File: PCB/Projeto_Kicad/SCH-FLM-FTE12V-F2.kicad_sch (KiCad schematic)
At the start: 17 parts, among them CN1 AKZ700-2-5,08V, CN2 AKZ700-2-5,08V, Q1 TIP120, Q2 BC547

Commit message: Atualização do resistor shunt R2 e R4
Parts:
- added R4: 0,22R/5W, Resistor_THT:R_Axial_DIN0516_L15.5mm_D5.0mm_P5.08mm_Vertical, symbol Device:R_US
- C1, C5: value 4700uF/25V -> 4700uF/35V
- R2: value 0,44R/5W -> 0,33R/5W
- RV1: value 10K -> 11K
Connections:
- net Vout: now also R4.2; no longer R2.2
- net +15V renamed +18V
- new net: R2.2, R4.1
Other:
- moved on the sheet: R2
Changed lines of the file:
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@@
+	)
+	(junction
+		(at 266.7 128.27)
+		(diameter 0)
+		(color 0 0 0 0)
 	)
 	(junction
@@
 	)
 	(junction
-		(at 299.72 128.27)
-		(diameter 0)
-		(color 0 0 0 0)
-	)
-	(junction
 		(at 220.98 154.94)
 		(diameter 0)
@@
 	)
 	(junction
-		(at 266.7 128.27)
-		(diameter 0)
-		(color 0 0 0 0)
-	)
-	(junction
 		(at 168.91 154.94)
 		(diameter 0)
@@
 	)
 	(junction
+		(at 299.72 128.27)
+		(diameter 0)
+		(color 0 0 0 0)
+	)
+	(junction
 		(at 199.39 139.7)
 		(diameter 0)
@@
 	(wire
 		(pts
+			(xy 279.4 128.27) (xy 287.02 128.27)
+		)
+		(stroke
+			(width 0)
+			(type default)
+		)
+	)
+	(wire
+		(pts
 			(xy 196.85 154.94) (xy 199.39 154.94)
 		)
@@
 	(wire
 		(pts
-			(xy 266.7 128.27) (xy 275.59 128.27)
+			(xy 266.7 128.27) (xy 271.78 128.27)
+		)
+		(stroke
+			(width 0)
+			(type default)
+		)
+	)
+	(wire
+		(pts
+			(xy 294.64 128.27) (xy 299.72 128.27)
 		)
 		(stroke
@@
 		(pts
 			(xy 177.8 148.59) (xy 177.8 154.94)
-		)
-		(stroke
-			(width 0)
-			(type default)
-		)
-	)
-	(wire
-		(pts
-			(xy 283.21 128.27) (xy 299.72 128.27)
 		)
 		(stroke
@@
 			)
 		)
-		(property "Value" "4700uF/25V"
+		(property "Value" "4700uF/35V"
 			(at 179.07 143.256 90)
 			(show_name no)
@@
 	(symbol
 		(lib_id "Device:R_US")
-		(at 279.4 128.27 90)
+		(at 290.83 128.27 90)
+		(unit 1)
+		(body_style 1)
+		(exclude_from_sim no)
+		(in_bom yes)
+		(on_board yes)
+		(in_pos_files yes)
+		(dnp no)
+		(property "Reference" "R4"
+			(at 290.322 125.476 90)
+			(show_name no)
+			(do_not_autoplace no)
+			(effects
+				(font
+					(size 1.5 1.5)
+				)
+			)
+		)
+		(property "Value" "0,22R/5W"
+			(at 290.83 130.81 90)
+			(show_name no)
+			(do_not_autoplace no)
+			(effects
+				(font
+					(size 1.5 1.5)
+				)
+			)
+		)
+		(property "Footprint" "Resistor_THT:R_Axial_DIN0516_L15.5mm_D5.0mm_P5.08mm_Vertical"
+			(at 291.084 127.254 90)
+			(hide yes)
+			(show_name no)
+			(do_not_autoplace no)
+			(effects
+				(font
+					(size 1.27 1.27)
+				)
+			)
+		)
+		(property "Datasheet" ""
+			(at 290.83 128.27 0)
+			(hide yes)
+			(show_name no)
+			(do_not_autoplace no)
+			(effects
+				(font
+					(size 1.27 1.27)
+				)
+			)
+		)
+		(property "Description" "Resistor, US symbol"
+			(at 290.83 128.27 0)
+			(hide yes)
+			(show_name no)
+			(do_not_autoplace no)
+			(effects
+				(font
+					(size 1.27 1.27)
+				)
+			)
+		)
+		(property "ALTIUM_VALUE" ""
+			(at 290.83 128.27 90)
+			(hide yes)
+			(show_name no)
+			(do_not_autoplace no)
+			(effects
+				(font
+					(size 1.27 1.27)
+				)
+			)
+		)
+		(pin "2"
+		)
+		(pin "1"
+		)
+		(instances
+			(project "PCB-FLM-FTE-12V"
+				(path "/24c863d3-5da9-46c2-adf2-885da2a6f9d5/4761fa84-89f9-48c7-be1e-a8eadc20ef8c"
+					(reference "R4")
+					(unit 1)
+				)
+			)
+		)
+	)
+	(symbol
+		(lib_id "Device:R_US")
+		(at 275.59 128.27 90)
 		(unit 1)
 		(body_style 1)
@@
 		(dnp no)
 		(property "Reference" "R2"
-			(at 278.892 125.476 90)
-			(show_name no)
-			(do_not_autoplace no)
-			(effects
-				(font
-					(size 1.5 1.5)
-				)
-			)
-		)
-		(property "Value" "0,44R/5W"
-			(at 279.4 130.81 90)
+			(at 275.082 125.476 90)
+			(show_name no)
+			(do_not_autoplace no)
+			(effects
+				(font
+					(size 1.5 1.5)
+				)
+			)
+		)
+		(property "Value" "0,33R/5W"
+			(at 275.59 130.81 90)
 			(show_name no)
 			(do_not_autoplace no)
@@
 		)
 		(property "Footprint" "Resistor_THT:R_Axial_DIN0516_L15.5mm_D5.0mm_P5.08mm_Vertical"
-			(at 279.654 127.254 90)
+			(at 275.844 127.254 90)
 			(hide yes)
 			(show_name no)
@@
 		)
 		(property "Datasheet" ""
-			(at 279.4 128.27 0)
+			(at 275.59 128.27 0)
 			(hide yes)
 			(show_name no)
@@
 		)
 		(property "Description" "Resistor, US symbol"
-			(at 279.4 128.27 0)
+			(at 275.59 128.27 0)
 			(hide yes)
 			(show_name no)
@@
 		)
 		(property "ALTIUM_VALUE" ""
-			(at 279.4 128.27 90)
+			(at 275.59 128.27 90)
 			(hide yes)
 			(show_name no)
@@
 			)
 		)
-		(property "Value" "+15V"
+		(property "Value" "+18V"
 			(at 188.976 119.38 0)
 			(show_name no)
@@
 			)
 		)
-		(property "Value" "4700uF/25V"
+		(property "Value" "4700uF/35V"
 			(at 187.96 143.256 90)
 			(show_name no)
@@
 			)
 		)
-		(property "Value" "10K"
+		(property "Value" "11K"
 			(at 219.202 146.304 0)
 			(show_name no)

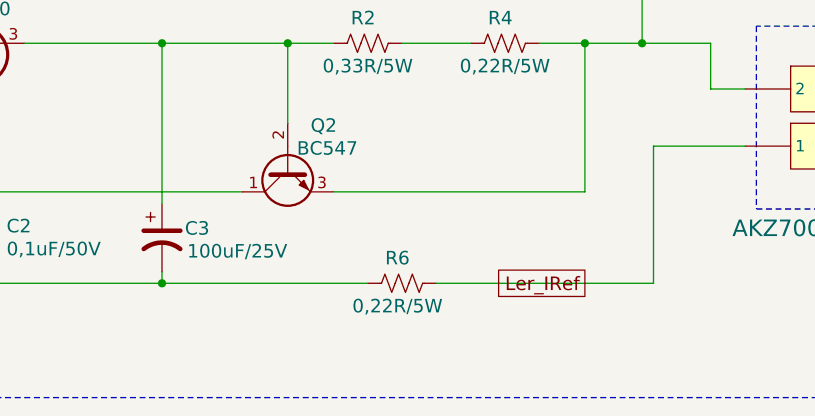
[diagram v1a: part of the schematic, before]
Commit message: Adição do R7 em paralelo com R6 e adição do RF2 de 15K e mudança de valor do RF1 de 10K para 15K
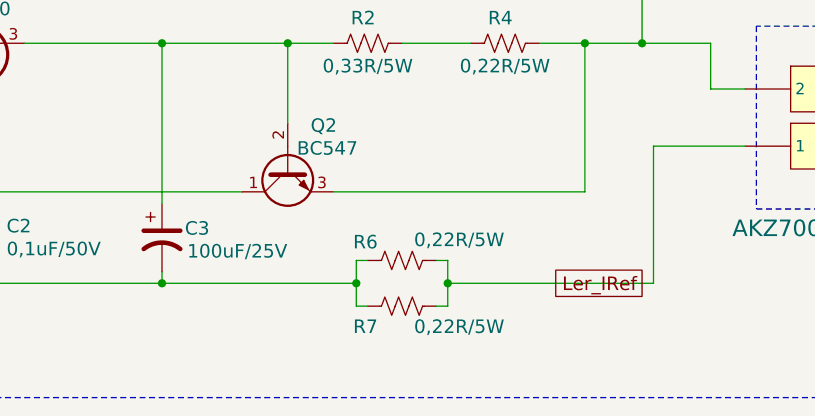
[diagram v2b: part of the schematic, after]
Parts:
- added R7: 0,22R/5W, Resistor_THT:R_Axial_DIN0516_L15.5mm_D5.0mm_P5.08mm_Vertical, symbol Device:R_US
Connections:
- net GND: now also R6.2, R7.2; no longer R6.1
- net Ler_IRef: now also R6.1, R7.1; no longer R6.2
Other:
- moved on the sheet: R6
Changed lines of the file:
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@@
+	)
+	(junction
+		(at 274.32 154.94)
+		(diameter 0)
+		(color 0 0 0 0)
 	)
 	(junction
@@
 	)
 	(junction
+		(at 189.23 128.27)
+		(diameter 0)
+		(color 0 0 0 0)
+	)
+	(junction
+		(at 168.91 154.94)
+		(diameter 0)
+		(color 0 0 0 0)
+	)
+	(junction
+		(at 232.41 154.94)
+		(diameter 0)
+		(color 0 0 0 0)
+	)
+	(junction
+		(at 154.94 137.16)
+		(diameter 0)
+		(color 0 0 0 0)
+	)
+	(junction
+		(at 168.91 143.51)
+		(diameter 0)
+		(color 0 0 0 0)
+	)
+	(junction
+		(at 177.8 154.94)
+		(diameter 0)
+		(color 0 0 0 0)
+	)
+	(junction
+		(at 177.8 128.27)
+		(diameter 0)
+		(color 0 0 0 0)
+	)
+	(junction
+		(at 284.48 154.94)
+		(diameter 0)
+		(color 0 0 0 0)
+	)
+	(junction
+		(at 232.41 144.78)
+		(diameter 0)
+		(color 0 0 0 0)
+	)
+	(junction
+		(at 186.69 154.94)
+		(diameter 0)
+		(color 0 0 0 0)
+	)
+	(junction
+		(at 306.07 128.27)
+		(diameter 0)
+		(color 0 0 0 0)
+	)
+	(junction
+		(at 199.39 128.27)
+		(diameter 0)
+		(color 0 0 0 0)
+	)
+	(junction
+		(at 299.72 128.27)
+		(diameter 0)
+		(color 0 0 0 0)
+	)
+	(junction
+		(at 199.39 139.7)
+		(diameter 0)
+		(color 0 0 0 0)
+	)
+	(junction
+		(at 199.39 154.94)
+		(diameter 0)
+		(color 0 0 0 0)
+	)
+	(junction
 		(at 252.73 154.94)
 		(diameter 0)
 		(color 0 0 0 0)
 	)
-	(junction
-		(at 189.23 128.27)
-		(diameter 0)
-		(color 0 0 0 0)
-	)
-	(junction
-		(at 168.91 154.94)
-		(diameter 0)
-		(color 0 0 0 0)
-	)
-	(junction
-		(at 232.41 154.94)
-		(diameter 0)
-		(color 0 0 0 0)
-	)
-	(junction
-		(at 154.94 137.16)
-		(diameter 0)
-		(color 0 0 0 0)
-	)
-	(junction
-		(at 168.91 143.51)
-		(diameter 0)
-		(color 0 0 0 0)
-	)
-	(junction
-		(at 177.8 154.94)
-		(diameter 0)
-		(color 0 0 0 0)
-	)
-	(junction
-		(at 177.8 128.27)
-		(diameter 0)
-		(color 0 0 0 0)
-	)
-	(junction
-		(at 232.41 144.78)
-		(diameter 0)
-		(color 0 0 0 0)
-	)
-	(junction
-		(at 186.69 154.94)
-		(diameter 0)
-		(color 0 0 0 0)
-	)
-	(junction
-		(at 306.07 128.27)
-		(diameter 0)
-		(color 0 0 0 0)
-	)
-	(junction
-		(at 199.39 128.27)
-		(diameter 0)
-		(color 0 0 0 0)
-	)
-	(junction
-		(at 299.72 128.27)
-		(diameter 0)
-		(color 0 0 0 0)
-	)
-	(junction
-		(at 199.39 139.7)
-		(diameter 0)
-		(color 0 0 0 0)
-	)
-	(junction
-		(at 199.39 154.94)
-		(diameter 0)
-		(color 0 0 0 0)
-	)
 	(wire
 		(pts
@@
 	(wire
 		(pts
-			(xy 283.21 154.94) (xy 307.34 154.94)
-		)
-		(stroke
-			(width 0)
-			(type default)
-		)
-	)
-	(wire
-		(pts
 			(xy 154.94 129.54) (xy 154.94 128.27)
 		)
@@
 	(wire
 		(pts
+			(xy 283.21 157.48) (xy 284.48 157.48)
+		)
+		(stroke
+			(width 0)
+			(type default)
+		)
+	)
+	(wire
+		(pts
 			(xy 232.41 154.94) (xy 232.41 153.67)
 		)
@@
 	(wire
 		(pts
+			(xy 274.32 157.48) (xy 275.59 157.48)
+		)
+		(stroke
+			(width 0)
+			(type default)
+		)
+	)
+	(wire
+		(pts
 			(xy 177.8 128.27) (xy 186.69 128.27)
 		)
@@
 	(wire
 		(pts
+			(xy 274.32 152.4) (xy 274.32 154.94)
+		)
+		(stroke
+			(width 0)
+			(type default)
+		)
+	)
+	(wire
+		(pts
 			(xy 279.4 128.27) (xy 287.02 128.27)
 		)
@@
 	(wire
 		(pts
+			(xy 252.73 154.94) (xy 274.32 154.94)
+		)
+		(stroke
+			(width 0)
+			(type default)
+		)
+	)
+	(wire
+		(pts
 			(xy 154.94 137.16) (xy 154.94 146.05)
 		)
@@
 	(wire
 		(pts
+			(xy 284.48 157.48) (xy 284.48 154.94)
+		)
+		(stroke
+			(width 0)
+			(type default)
+		)
+	)
+	(wire
+		(pts
 			(xy 186.69 154.94) (xy 196.85 154.94)
 		)
@@
 	(wire
 		(pts
-			(xy 252.73 154.94) (xy 275.59 154.94)
+			(xy 284.48 154.94) (xy 284.48 152.4)
 		)
 		(stroke
@@
 	(wire
 		(pts
+			(xy 274.32 154.94) (xy 274.32 157.48)
+		)
+		(stroke
+			(width 0)
+			(type default)
+		)
+	)
+	(wire
+		(pts
 			(xy 189.23 128.27) (xy 199.39 128.27)
 		)
@@
 	(wire
 		(pts
+			(xy 284.48 152.4) (xy 283.21 152.4)
+		)
+		(stroke
+			(width 0)
+			(type default)
+		)
+	)
+	(wire
+		(pts
+			(xy 284.48 154.94) (xy 307.34 154.94)
+		)
+		(stroke
+			(width 0)
+			(type default)
+		)
+	)
+	(wire
+		(pts
 			(xy 299.72 128.27) (xy 299.72 144.78)
 		)
@@
 		(pts
 			(xy 144.78 143.51) (xy 168.91 143.51)
+		)
+		(stroke
+			(width 0)
+			(type default)
+		)
+	)
+	(wire
+		(pts
+			(xy 275.59 152.4) (xy 274.32 152.4)
 		)
 		(stroke
@@
 	(global_label "Ler_IRef"
 		(shape passive)
-		(at 299.72 154.94 180)
+		(at 306.07 154.94 180)
 		(fields_autoplaced yes)
 		(effects
@@
 		)
 		(property "Intersheetrefs" "${INTERSHEET_REFS}"
-			(at 288.5786 154.94 0)
+			(at 294.9286 154.94 0)
 			(hide yes)
 			(show_name no)
@@
 	)
 	(symbol
+		(lib_id "Device:R_US")
+		(at 279.4 157.48 270)
+		(unit 1)
+		(body_style 1)
+		(exclude_from_sim no)
+		(in_bom yes)
+		(on_board yes)
+		(in_pos_files yes)
+		(dnp no)
+		(property "Reference" "R7"
+			(at 275.336 159.766 90)
+			(show_name no)
+			(do_not_autoplace no)
+			(effects
+				(font
+					(size 1.5 1.5)
+				)
+			)
+		)
+		(property "Value" "0,22R/5W"
+			(at 285.75 159.766 90)
+			(show_name no)
+			(do_not_autoplace no)
+			(effects
+				(font
+					(size 1.5 1.5)
+				)
+			)
+		)
+		(property "Footprint" "Resistor_THT:R_Axial_DIN0516_L15.5mm_D5.0mm_P5.08mm_Vertical"
+			(at 279.146 158.496 90)
+			(hide yes)
+			(show_name no)
+			(do_not_autoplace no)
+			(effects
+				(font
+					(size 1.27 1.27)
+				)
+			)
+		)
+		(property "Datasheet" ""
+			(at 279.4 157.48 0)
+			(hide yes)
+			(show_name no)
+			(do_not_autoplace no)
+			(effects
+				(font
+					(size 1.27 1.27)
+				)
+			)
+		)
+		(property "Description" "Resistor, US symbol"
+			(at 279.4 157.48 0)
+			(hide yes)
+			(show_name no)
+			(do_not_autoplace no)
+			(effects
+				(font
+					(size 1.27 1.27)
+				)
+			)
+		)
+		(property "ALTIUM_VALUE" ""
+			(at 279.4 157.48 90)
+			(hide yes)
+			(show_name no)
+			(do_not_autoplace no)
+			(effects
+				(font
+					(size 1.27 1.27)
+				)
+			)
+		)
+		(pin "2"
+		)
+		(pin "1"
+		)
+		(instances
+			(project "PCB-FLM-FTE-12V"
+				(path "/24c863d3-5da9-46c2-adf2-885da2a6f9d5/4761fa84-89f9-48c7-be1e-a8eadc20ef8c"
+					(reference "R7")
+					(unit 1)
+				)
+			)
+		)
+	)
+	(symbol
 		(lib_id "SCH-DISCRETO:GND1_POWER_GROUND")
 		(at 196.85 157.48 0)
@@
 	(symbol
 		(lib_id "Device:R_US")
-		(at 279.4 154.94 90)
+		(at 279.4 152.4 270)
 		(unit 1)
 		(body_style 1)
@@
 		(dnp no)
 		(property "Reference" "R6"
-			(at 278.892 152.146 90)
+			(at 275.336 150.368 90)
 			(show_name no)
 			(do_not_autoplace no)
@@
 		)
 		(property "Value" "0,22R/5W"
-			(at 278.892 157.48 90)
+			(at 285.75 150.114 90)
 			(show_name no)
 			(do_not_autoplace no)
@@
 		)
 		(property "Footprint" "Resistor_THT:R_Axial_DIN0516_L15.5mm_D5.0mm_P5.08mm_Vertical"
-			(at 279.654 153.924 90)
+			(at 279.146 153.416 90)
 			(hide yes)
 			(show_name no)
@@
 		)
 		(property "Datasheet" ""
-			(at 279.4 154.94 0)
+			(at 279.4 152.4 0)
 			(hide yes)
 			(show_name no)
@@
 		)
 		(property "Description" "Resistor, US symbol"
-			(at 279.4 154.94 0)
+			(at 279.4 152.4 0)
 			(hide yes)
 			(show_name no)
@@
 		)
 		(property "ALTIUM_VALUE" ""
-			(at 279.4 154.94 90)
-			(hide yes)
-			(show_name no)
+			(at 279.4 152.4 90)
+			(hide yes)
+			(show_name no)

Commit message: Atualização do esquemático - R7 opcional
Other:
- note added: "OPCIONAL"
- moved on the sheet: R6, R7
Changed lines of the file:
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@@
+	)
+	(rectangle
+		(start 269.24 156.845)
+		(end 293.37 165.1)
+		(stroke
+			(width 0.3)
+			(type dot)
+		)
+		(fill
+			(type none)
+		)
 	)
 	(rectangle
@@
 		)
 	)
+	(text "OPCIONAL"
+		(exclude_from_sim no)
+		(at 299.212 164.592 0)
+		(effects
+			(font
+				(size 1.5 1.5)
+			)
+		)
+	)
 	(junction
 		(at 266.7 128.27)
@@
 	(wire
 		(pts
-			(xy 283.21 157.48) (xy 284.48 157.48)
+			(xy 283.21 160.02) (xy 284.48 160.02)
 		)
 		(stroke
@@
 	(wire
 		(pts
-			(xy 274.32 157.48) (xy 275.59 157.48)
+			(xy 274.32 160.02) (xy 275.59 160.02)
 		)
 		(stroke
@@
 	(wire
 		(pts
-			(xy 274.32 152.4) (xy 274.32 154.94)
+			(xy 274.32 149.86) (xy 274.32 154.94)
 		)
 		(stroke
@@
 	(wire
 		(pts
-			(xy 284.48 157.48) (xy 284.48 154.94)
+			(xy 284.48 160.02) (xy 284.48 154.94)
 		)
 		(stroke
@@
 	(wire
 		(pts
-			(xy 284.48 154.94) (xy 284.48 152.4)
+			(xy 284.48 154.94) (xy 284.48 149.86)
 		)
 		(stroke
@@
 	(wire
 		(pts
-			(xy 274.32 154.94) (xy 274.32 157.48)
+			(xy 274.32 154.94) (xy 274.32 160.02)
 		)
 		(stroke
@@
 	(wire
 		(pts
-			(xy 284.48 152.4) (xy 283.21 152.4)
+			(xy 284.48 149.86) (xy 283.21 149.86)
 		)
 		(stroke
@@
 	(wire
 		(pts
-			(xy 275.59 152.4) (xy 274.32 152.4)
+			(xy 275.59 149.86) (xy 274.32 149.86)
 		)
 		(stroke
@@
 	(symbol
 		(lib_id "Device:R_US")
-		(at 279.4 157.48 270)
+		(at 279.4 160.02 270)
 		(unit 1)
 		(body_style 1)
@@
 		(dnp no)
 		(property "Reference" "R7"
-			(at 275.336 159.766 90)
+			(at 275.336 162.306 90)
 			(show_name no)
 			(do_not_autoplace no)
@@
 		)
 		(property "Value" "0,22R/5W"
-			(at 285.75 159.766 90)
+			(at 285.75 162.306 90)
 			(show_name no)
 			(do_not_autoplace no)
@@
 		)
 		(property "Footprint" "Resistor_THT:R_Axial_DIN0516_L15.5mm_D5.0mm_P5.08mm_Vertical"
-			(at 279.146 158.496 90)
+			(at 279.146 161.036 90)
 			(hide yes)
 			(show_name no)
@@
 		)
 		(property "Datasheet" ""
-			(at 279.4 157.48 0)
+			(at 279.4 160.02 0)
 			(hide yes)
 			(show_name no)
@@
 		)
 		(property "Description" "Resistor, US symbol"
-			(at 279.4 157.48 0)
+			(at 279.4 160.02 0)
 			(hide yes)
 			(show_name no)
@@
 		)
 		(property "ALTIUM_VALUE" ""
-			(at 279.4 157.48 90)
+			(at 279.4 160.02 90)
 			(hide yes)
 			(show_name no)
@@
 	(symbol
 		(lib_id "Device:R_US")
-		(at 279.4 152.4 270)
+		(at 279.4 149.86 270)
 		(unit 1)
 		(body_style 1)
@@
 		(dnp no)
 		(property "Reference" "R6"
-			(at 275.336 150.368 90)
+			(at 275.336 147.828 90)
 			(show_name no)
 			(do_not_autoplace no)
@@
 		)
 		(property "Value" "0,22R/5W"
-			(at 285.75 150.114 90)
+			(at 285.75 147.574 90)
 			(show_name no)
 			(do_not_autoplace no)
@@
 		)
 		(property "Footprint" "Resistor_THT:R_Axial_DIN0516_L15.5mm_D5.0mm_P5.08mm_Vertical"
-			(at 279.146 153.416 90)
+			(at 279.146 150.876 90)
 			(hide yes)
 			(show_name no)
@@
 		)
 		(property "Datasheet" ""
-			(at 279.4 152.4 0)
+			(at 279.4 149.86 0)
 			(hide yes)
 			(show_name no)
@@
 		)
 		(property "Description" "Resistor, US symbol"
-			(at 279.4 152.4 0)
+			(at 279.4 149.86 0)
 			(hide yes)
 			(show_name no)
@@
 		)
 		(property "ALTIUM_VALUE" ""
-			(at 279.4 152.4 90)
-			(hide yes)
-			(show_name no)
+			(at 279.4 149.86 90)
+			(hide yes)
+			(show_name no)
